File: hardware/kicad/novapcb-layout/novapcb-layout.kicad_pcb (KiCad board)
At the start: 4 copper layers, 36 x 36 mm, 70 parts, among them J1 USB-C_2.0, J10 CRSF_4P, J11 ESC_solder_pad, J12 ESC_solder_pad, J13 ESC_solder_pad, J14 ESC_solder_pad, J15 ESC_solder_pad, J16 ESC_solder_pad, J17 ESC_solder_pad, J18 ESC_solder_pad, J2 microSD_DM3AT, J3 TELEM_6P, J4 MAUCH_6P, J5 GPS_MAG_10P, J9 SWD_10P, U1 STM32H743VITx, U2 AP2112K-3.3, U3 ICM-42688-P, U4 DPS310, U5 USBLC6-2P6, Y1 8MHz

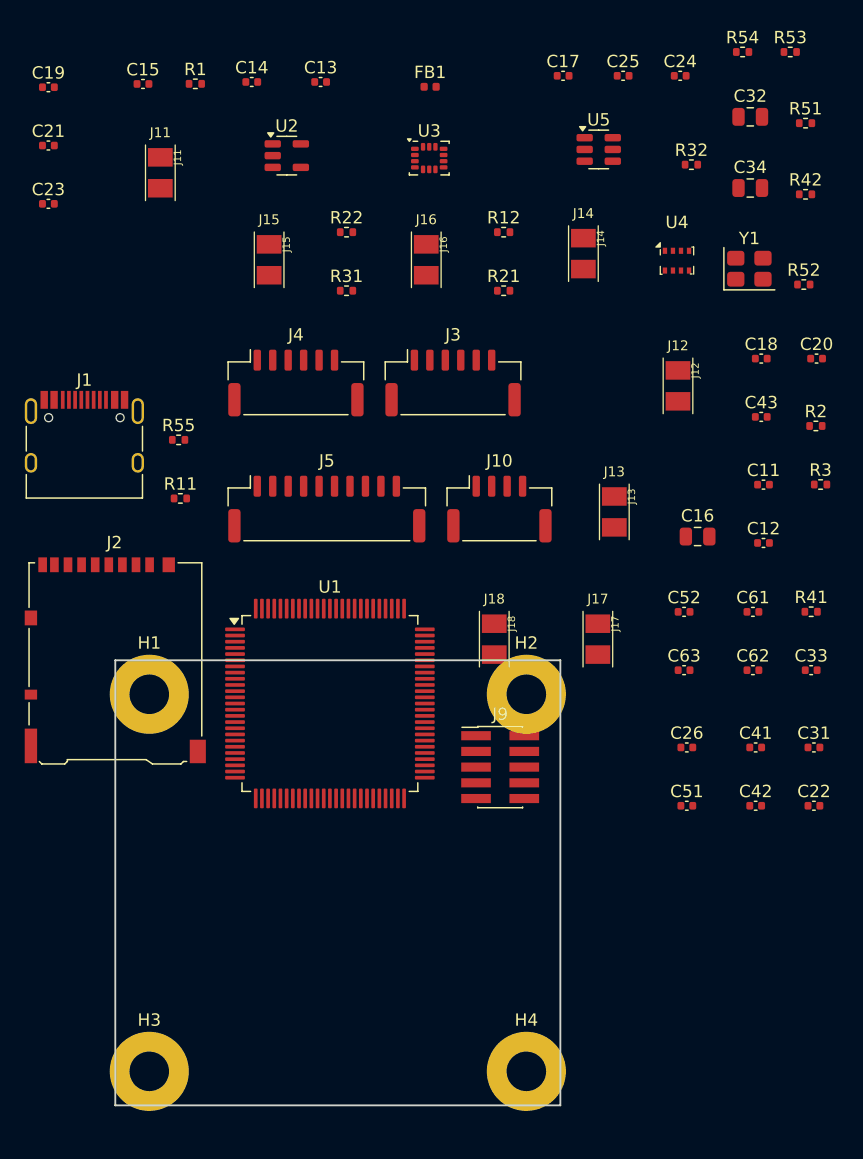
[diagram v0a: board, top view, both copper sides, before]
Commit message: Phase 4b implementation — placement step + ICM-42688-P carry-forward
Companion to phase-4b-placement.yaml contract:

- generate_board.py: PLACEMENT step (per-component-group, reasoned)
  + project file SoT (rewrites .kicad_pro from script so kicad-cli
  doesn't trample net classes + DRC severities)
- novapcb-layout.kicad_pcb: regenerated with all 70 components placed
- novapcb-layout.kicad_pro: net classes + DRC severities + rule overrides
  (Default 0.15mm clearance + 4-layer rules)
- OPEN_QUESTIONS.md: phase4a-1 entry — ICM-42688-P HARD carry-forward
  must-resolve-before-Phase-6m (master 4a adjudication)
- DESIGN_PHASES.md: Phase 4a row → DONE with phase4a-1 carry-forward
  note; Phase 4b row → DONE (first-pass headless)

Co-Authored-By: Claude Opus 4.7 <noreply@anthropic.com>
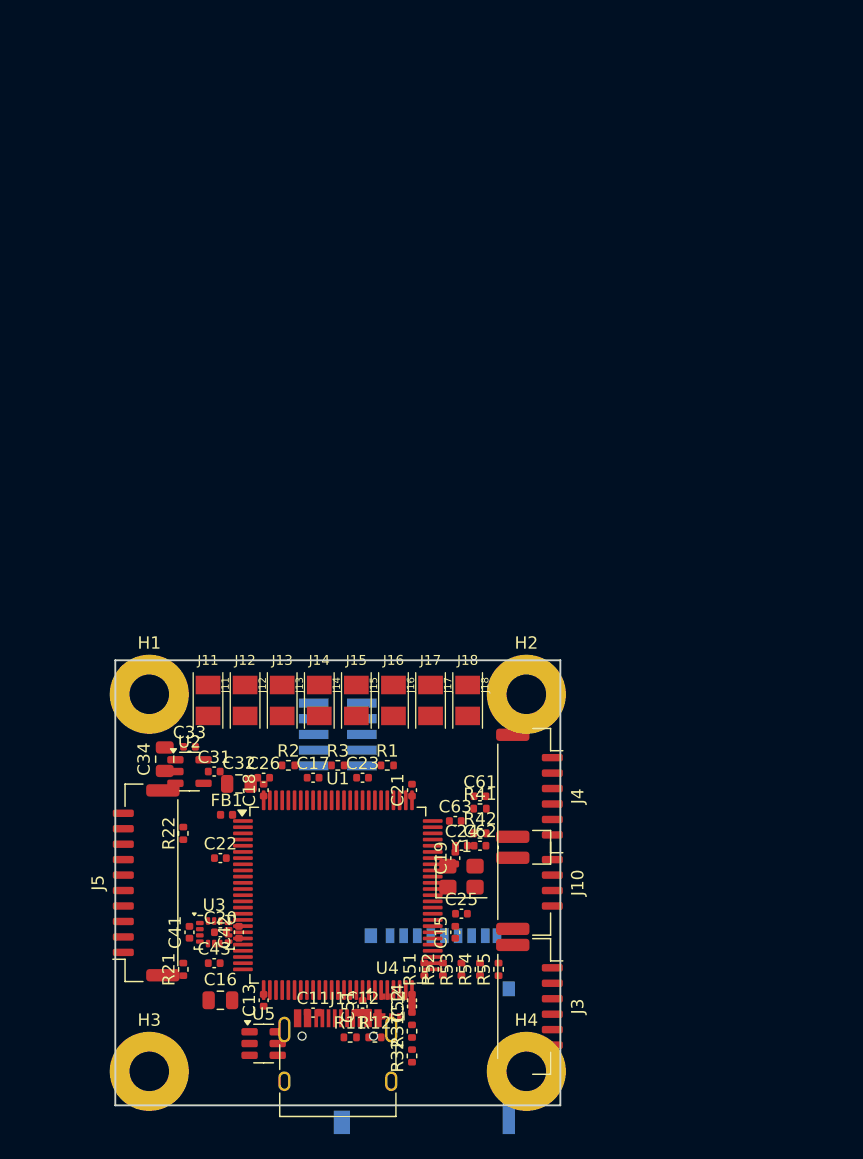
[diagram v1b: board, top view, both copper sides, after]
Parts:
- J2, J9: moved to B.Cu
- moved R53 78.8 mm to (28.0, 25.0), turned to 90 degrees
- moved U5 77.2 mm to (12.0, 31.0)
- moved R54 77.2 mm to (29.5, 25.0), turned to 90 degrees
- moved R32 75.5 mm to (24.0, 32.0), turned to 90 degrees
- moved C14 75.4 mm to (24.0, 27.5), turned to 90 degrees
- moved R51 75.1 mm to (25.0, 25.0), turned to 90 degrees
- moved C13 74.4 mm to (12.0, 27.5), turned to 90 degrees
- moved C15 73.1 mm to (27.5, 22.0), turned to 90 degrees
- moved C19 70.5 mm to (27.5, 16.0), turned to 90 degrees
- moved C25 69.0 mm to (28.0, 20.5)
- moved C32 68.0 mm to (10.0, 10.0)
- moved C20 66.9 mm to (8.50, 22.0)
- moved C34 66.2 mm to (4.00, 8.00), turned to 90 degrees
- moved R12 66.0 mm to (21.0, 30.5)
- moved U3 65.0 mm to (8.00, 22.0)
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
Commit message: Phase 4b-rev: finer-precision pass (87 -> 18 DRC violations; 79% reduction)
Per master Phase 4b adjudication: rejecting "clean A" and "wholesale GUI
B"; applying targeted rev. Real finer-precision pass on the 1.0mm-grid
placement, structural microSD fix, U4 baro flip to B.Cu.

## Master 4b-rev scope items

### 1. microSD structural fix ✓

J2 moved from (25, 30) B.Cu (where THT keep-out clipped H4 + J1) to
(18, 6) B.Cu (center-south). Body Y=0.5..11.5 clears MCU body Y=12..26
by 0.5mm. Keep-out X=10..26, Y=-3..19 clears all THT positions:
H1/H2/H3/H4 mounting pads + J1 USB-C shield pads at (13.68/22.32, 29.87).
J9 SWD moved to (18, 21) B.Cu to clear J2 keep-out.

Result: 4 items_not_allowed + hole_clearance violations → **0**. ✓

### 2. Finer-precision placement pass (1mm grid -> targeted 0.1mm nudges)

Real measurements of MCU U1 pad outer extents (W X=9.52, E X=26.48,
N Y=27.48, S Y=10.52) used to compute required passive clearances.

Key moves:
- U3 IMU moved west from (8,22) -> (6,22) — was overlapping MCU west
  pads by 0.05mm (IMU east outer X=9.47 vs MCU west outer X=9.52);
  now 2.05mm gap
- C11/C12 moved out of J1 USB-C body X-range (J1 X=14.55..21.45);
  N-side decoupling now at (12.5/23.5, 28.5)
- C13/C14 moved further to corners (10.5/25.5, 27.5)
- Y1 crystal moved east 1.5mm (28 -> 29.5) to clear MCU east pads
- C19 + C24/C25 follow Y1; C19 moved S of Y1 body
- C18/C21/R1/R2/R3 moved south of MCU S pad outer Y=10.52
- R11/R12 I2C2 pull-ups moved to NW/NE clear of MCU + J1
- R51-R55 SDMMC pullups shifted right of MCU east pads
- ADC filter cluster (R41/R42/C61/C62/C63) moved west of Y1 column

### 3. U4 DPS310 structurally flipped to B.Cu

F.Cu has no room between MCU N pad outer (Y=27.48) and J1 USB-C body
south (Y=29.35) — gap only 1.87mm vs U4 body 2.5mm. NOT a precision
issue — a real space conflict. Master "Rule 13 stop" trigger; resolved
by structural decision: U4 on B.Cu at (22, 28). C51/C52 decoupling also
flipped to B.Cu to follow U4. Phase 4d ro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
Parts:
- C51, C52, U4: moved to B.Cu
- moved J2 25.0 mm to (18.0, 6.00)
- moved J9 15.0 mm to (18.0, 21.0)
- moved R11 10.7 mm to (8.50, 28.5), turned to 90 degrees
- moved R12 6.80 mm to (27.5, 28.5), turned to 90 degrees
- moved C63 4.03 mm to (29.5, 9.50)
- moved C43 4.00 mm to (4.00, 24.5)
- moved C42 3.61 mm to (8.00, 25.0), turned to 0 degrees
- moved C11 3.50 mm to (12.5, 28.5)
- moved C12 3.50 mm to (23.5, 28.5)
- moved R51 2.69 mm to (27.5, 24.0)
- moved R52 2.69 mm to (29.0, 24.0)
- moved R53 2.69 mm to (30.5, 24.0)
- moved R54 2.69 mm to (32.0, 24.0)
- moved R55 2.69 mm to (33.5, 24.0)
- moved C16 2.50 mm to (6.00, 27.5)
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
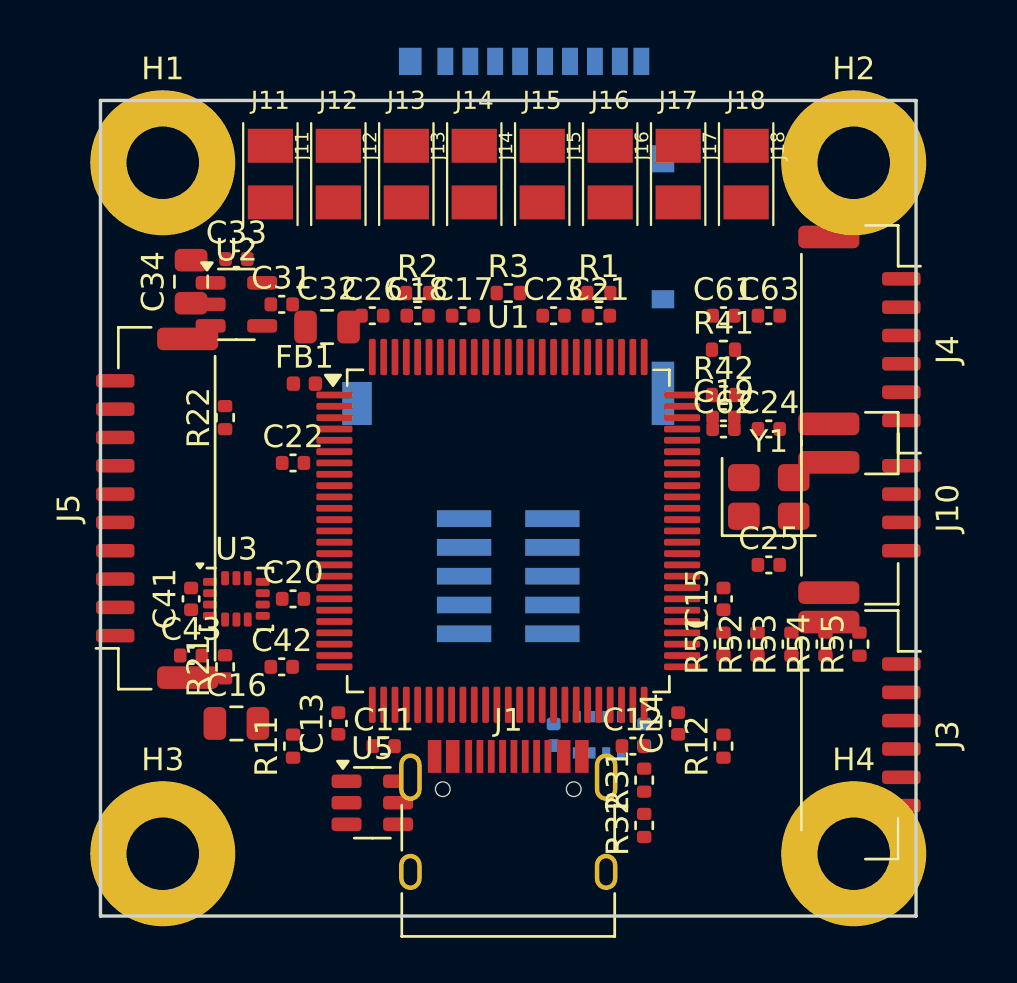
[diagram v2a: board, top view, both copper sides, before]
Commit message: Phase 4c: copper plane pour (Rule 13 stop at 4c.6) (#44)
* Phase 4c: copper plane pour (Rule 13 stop at 4c.6 — 5 shorts persist)

Plane pour implemented per master's iter-#3 P0 pre-conditions. 4c.6
DRC re-check triggers Rule 13 stop per master's 4b adjudication
("If any do NOT resolve, that's a Rule 13 stop").

## What got done

7 copper zones added + persisted in .kicad_pcb:
- In1.Cu  GND   solid pour (full board minus 0.2mm edge inset)
- In2.Cu  +3V3  dominant (full board, low priority)
- In2.Cu  +5V   top band (Y>22): USB-C + N half of right edge
- In2.Cu  +5V   LDO strip (SW corner): U2 input
- In2.Cu  VBAT  small rect (S of MCU + J4 Mauch)
- In2.Cu  +3V3A tiny zone (MCU VDDA via FB1)
- B.Cu    GND   fill in unused areas (signal+GND-fill per fork)

DRC result:
- unconnected_items: 193 → 0 ✓ (planes connecting pads correctly)
- shorting_items: 5 → 5 (UNCHANGED — F.Cu pad-pad physical overlaps,
  plane pour on inner layers doesn't move pads)
- clearance: 13 (unchanged from 4b-rev)
- total: 18 (same as 4b-rev; planes didn't add violations but didn't
  resolve the shorts either)

## Rule 13 stop — 5 unresolved shorting_items

The 4b assumption "cap-GND shorts auto-resolve at 4c plane pour" was
WRONG. All 5 persist because they're F.Cu pad-pad physical overlaps:

1. U2 LDO pad-2 [GND] @ (4.86,9.00) ↔ C34 pad-1 [+3V3] @ (4.00,8.95)
2. U5 pad-5 [+5V] @ (13.14,31.00) ↔ J1 USB-C PTH shield [GND] @ (13.68,29.87)
3. U5 pad-6 [USB_DP] @ (13.14,30.05) ↔ J1 shield same position
4. C62 [BATT_CURRENT_SENS] @ (27.02,14.50) ↔ C19 [+3V3A] @ (27.02,14.00)
5. C26 [NRST] @ (11.52,9.50) ↔ C32 [GND] @ (10.95,10.00)

All 5 fixable by ~1-2mm targeted nudges (worker did NOT apply — 4c
scope is planes, not placement). Master adjudicates options A/B/C in
phase-4c-planes.yaml escalation_log #1; worker recommends B (4b-rev3
targeted nudges on the 5 specific F.Cu pad collisions).

## Two pcbnew Python binding bugs discovered + worked around

Both logged in KICAD9_NOTES.md (cross-machine source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
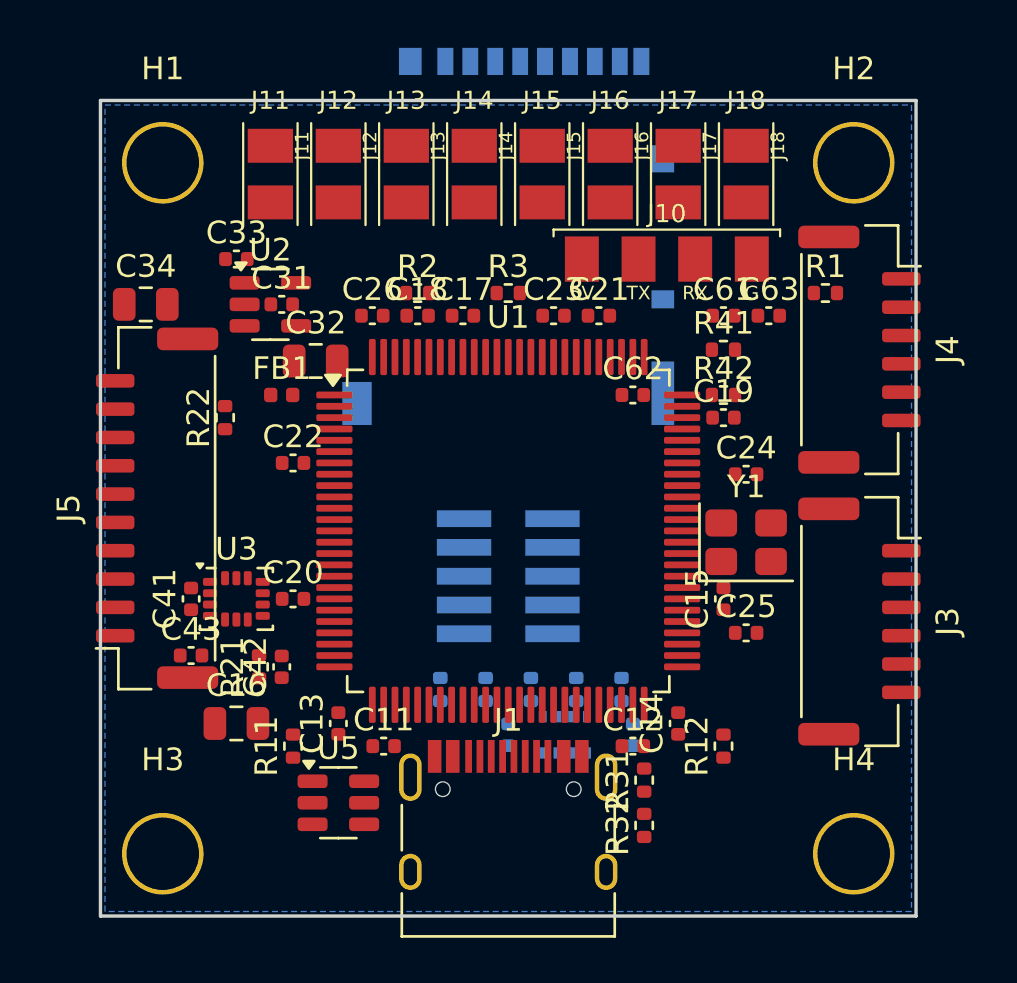
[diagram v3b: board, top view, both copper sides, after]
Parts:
- J10: value CRSF_4P -> CRSF_solder_pad; footprint Connector_JST:JST_GH_SM04B-GHS-TB_1x04-1MP_P1.25mm_Horizontal -> CRSF_solder_pad
- R51, R52, R53, R54, R55: moved to B.Cu
- moved J10 13.9 mm to (25.0, 7.00), turned to 0 degrees
- moved R51 12.7 mm to (15.0, 26.0)
- moved R52 12.2 mm to (17.0, 26.0)
- moved R53 11.7 mm to (19.0, 26.0)
- moved R54 11.2 mm to (21.0, 26.0)
- moved R55 10.7 mm to (23.0, 26.0)
- moved R1 10.0 mm to (32.0, 8.50)
- moved J3 5.00 mm to (33.5, 23.0)
- moved C62 4.27 mm to (23.5, 13.0)
- moved C25 3.16 mm to (28.5, 23.5)
- moved C24 2.24 mm to (28.5, 16.5)
- moved C34 2.24 mm to (2.00, 9.00), turned to 0 degrees
- moved Y1 2.24 mm to (28.5, 19.5)
- moved C51 2.00 mm to (18.0, 28.0)
- moved C32 1.58 mm to (9.50, 11.5)
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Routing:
- added copper zone on In2.Cu, net +3V3
- added copper zone on In2.Cu, net +3V3A
- added copper zone on In2.Cu, net +5V
- added copper zone on B.Cu, net GND
- added copper zone on In1.Cu, net GND
- added copper zone on In2.Cu, net VBAT
